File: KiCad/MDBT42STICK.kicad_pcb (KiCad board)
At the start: 2 copper layers, 78.4 x 40 mm, 22 parts, among them P1 CONN_01X04, P12 SERIALBUS, P2 USB_B, P3 CONN_01X07, P4 CONN_01X01, P5 CONN_01X03, SW1 RESET, U1 ADMP401Module, U2 MDBT42, U3 addressableLEDchip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

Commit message: 2nd version.
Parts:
- removed the C1 at (76.6, 78.7)
- removed C5: 0.1uF, Capacitors_SMD:C_0603
- removed P12: SERIALBUS, library:SolderWirePad_Circle_5xInline_0-8mmDrill
- removed the P2 at (116.2, 81.9)
- removed the P3 at (87.8, 89.9)
- removed P5: CONN_01X03, TO_SOT_Packages_THT:TO-43_3Pin
- removed SW1: RESET, Pin_Headers:Pin_Header_Straight_1x02
- removed U9: addressableLEDchip, library:addressableLEDchip3535
- added C1: 0.1uF, Capacitors_SMD:C_0603, F.Cu at (78.2, 79.3)
- added C1: 0.1, Capacitors_SMD:C_0603, F.Cu at (4.79, 74.9)
- added C2: 10, Capacitors_SMD:C_0603, F.Cu at (4.79, 88.5)
- added OSHW: 1.1, library:OSHW_LOGL_SYLK_5mm, F.Cu at (127.7, 82.5)
- added OSHW: 1.1, library:OSHW_LOGL_SYLK_5mm, F.Cu at (139.1, 82.7)
- added OSHW: 1.1, library:OSHW_LOGL_SYLK_5mm, F.Cu at (-6.41, 81.7)
- added P1: CONN_01X10, Connectors_Molex:Connector_Molex_PicoBlade_53047-1010, F.Cu at (-0.41, 75.7)
- added P2: CONN_01X08, library:SolderWirePad_Circle_8xInline_0-85mmDrill, F.Cu at (80.1, 87.6)
- added P2: CONN_01X05, Connectors_Molex:Connector_Molex_PicoBlade_53047-0510, F.Cu at (10.2, 89.9)
- added P3: OLED_0.96in_SPI, library:SolderWirePad_Circle_7xInline_0-85mmDrill, F.Cu at (61.0, 77.4)
- added P3: CONN_01X04, library:Grove_I2C_Horisontal_4pin_2mmpitch, F.Cu at (13.6, 81.7)
- added R1: 4.7k, Resistors_SMD:R_0603, F.Cu at (12.2, 72.9)
- added R2: 4.7k, Resistors_SMD:R_0603, F.Cu at (12.2, 75.1)
- added R3: 1.8k, Resistors_SMD:R_0603, F.Cu at (15.8, 72.9)
- added R4: 1.8k, Resistors_SMD:R_0603, F.Cu at (15.8, 75.1)
- added R5: 20k, Resistors_SMD:R_0603, F.Cu at (6.39, 90.7)
- added REF**: SolderWirePad_single_1-2mmDrill, Wire_Pads:SolderWirePad_single_1-2mmDrill, F.Cu at (26.1, 81.9)
- added U1: MTCH6102_SSOP28, Housings_SSOP:TSSOP-28_4.4x9.7mm_Pitch0.65mm, F.Cu at (6.59, 81.7)
- added U4: CP2102_Module, library:CP2102Module, F.Cu at (40.4, 82.2)
- C3, C4: footprint library:C_1206_HandSoldering_Small -> Capacitors_SMD:C_0603
- D1: footprint Diodes_SMD:MELF_Standard -> Diodes_SMD:TUMD2
- U5: value MPU-6500_Module -> GY-LSM6DS3Module; footprint library:MPU-6500_GY-6500 -> library:GY-LSM6DS3Module
- moved U6 68.9 mm to (36.6, 82.2), turned to 0 degrees
- moved U3 56.6 mm to (51.1, 71.2), turned to 0 degrees
- moved BT1 52.1 mm to (53.4, 85.1)
- moved C3 47.5 mm to (59.3, 79.9)
- moved U7 41.1 mm to (54.4, 81.7), turned to 90 degrees
- moved U1 25.4 mm to (73.7, 82.5), turned to 270 degrees
- moved C4 20.8 mm to (75.1, 79.3), turned to 0 degrees
- moved P1 10.4 mm to (71.2, 77.4)
- moved SP1 9.03 mm to (64.6, 83.2), turned to 90 degrees
- moved P4 7.73 mm to (59.1, 82.5)
- moved D1 6.02 mm to (58.8, 85.7)
- moved U5 4.79 mm to (61.0, 82.5), turned to 90 degrees
- moved U8 1.80 mm to (75.0, 83.1)
- moved U2 1.37 mm to (87.0, 81.2)
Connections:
- BT1 pad 2: GND -> Net-(BT1-Pad2)
- D1 pad 1: Net-(BT1-Pad1) -> Net-(D1-Pad1)
- D1 pad 2: Net-(D1-Pad2) -> Net-(BT1-Pad2)
- P4 pad 1: Net-(D1-Pad2) -> Net-(D1-Pad1)
- U2 pad 30: Net-(P12-Pad2) -> Net-(SW1-Pad2)
- U2 pad 35: Net-(SW1-Pad2) -> Net-(U2-Pad35)
- U5 pad 1: +3V3 -> Net-(BT1-Pad1)
- U5 pad 2: GND -> +3V3
- U5 pad 3: Net-(U2-Pad20) -> GND
- U5 pad 4: Net-(U2-Pad31) -> Net-(U2-Pad20)
- U5 pad 5: Net-(U5-Pad5) -> Net-(U2-Pad31)
- U5 pad 6: Net-(U5-Pad6) -> Net-(U2-Pad17)
- U5 pad 7: Net-(U5-Pad7) -> Net-(U2-Pad16)
- U6 pad 1: +5V -> Net-(U4-Pad3)
- U6 pad 4: GND -> Net-(BT1-Pad1)
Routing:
- net Net-(U2-Pad35): track 0.00 -> 49.9 mm, vias 0 -> 1
- net +3V3: track 113.0 -> 66.0 mm, vias 6 -> 1
- net Net-(P3-Pad3): track 29.0 -> 74.1 mm, vias 2 -> 4
- net Net-(C1-Pad1): track 0.00 -> 44.9 mm, vias 0 -> 2
- net Net-(SW1-Pad2): track 35.9 -> 0.00 mm, vias 4 -> 0
- net Net-(C1-Pad2): track 0.00 -> 34.6 mm
- net GND: track 174.0 -> 139.6 mm, vias 5 -> 10
- net Net-(BT1-Pad1): track 57.5 -> 25.6 mm, vias 1 -> 0
- net Net-(U2-Pad29): track 16.5 -> 46.3 mm
- net Net-(U4-Pad3): track 0.00 -> 28.9 mm
- net Net-(U2-Pad17): track 0.00 -> 27.8 mm, vias 0 -> 1
- net Net-(P3-Pad4): track 29.7 -> 57.0 mm, vias 2 -> 3
- net Net-(U2-Pad16): track 0.00 -> 26.7 mm, vias 0 -> 1
- net Net-(P2-Pad5): track 10.2 -> 33.3 mm, vias 2 -> 3
- net Net-(P2-Pad1): track 14.1 -> 35.5 mm, vias 1 -> 2
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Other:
- board size 78.4 x 40 mm -> 159 x 31 mm
- board text added: "00SCL 03SDA 06CS 08SA0"
- board text added: "01 03A1 04A2 05A3 07 09 10 11"
- board text added: "3V3 GND"
- board text added: "3V3 GND +5V ▲RX ▼TX DTR"
- board text added: "3V3 GND +5V ▼RX ▲TX DTR"
- board text added: "B+ B-"
- board text added: "CLK 3V3 DIO GND"
- board text added: "GND SIO 3.3 CLK"
- board text added: "MISO MOSI"
- board text added: "SCL MISO RST MOSI SCK"
- board text added: "SPI OLED Module"
- board text added: "ST-Link"
- board text added: "VIN 3V3 GND"
- board text added: "▼31A7"
- board text added: "▼Breadboard"
- board text added: "▼GYLOModule"
- board text added: "▼Speaker"
- board text removed: "GND 3V3 5NC RX TX"
- board text removed: "GND CLK 3.3 SIO"

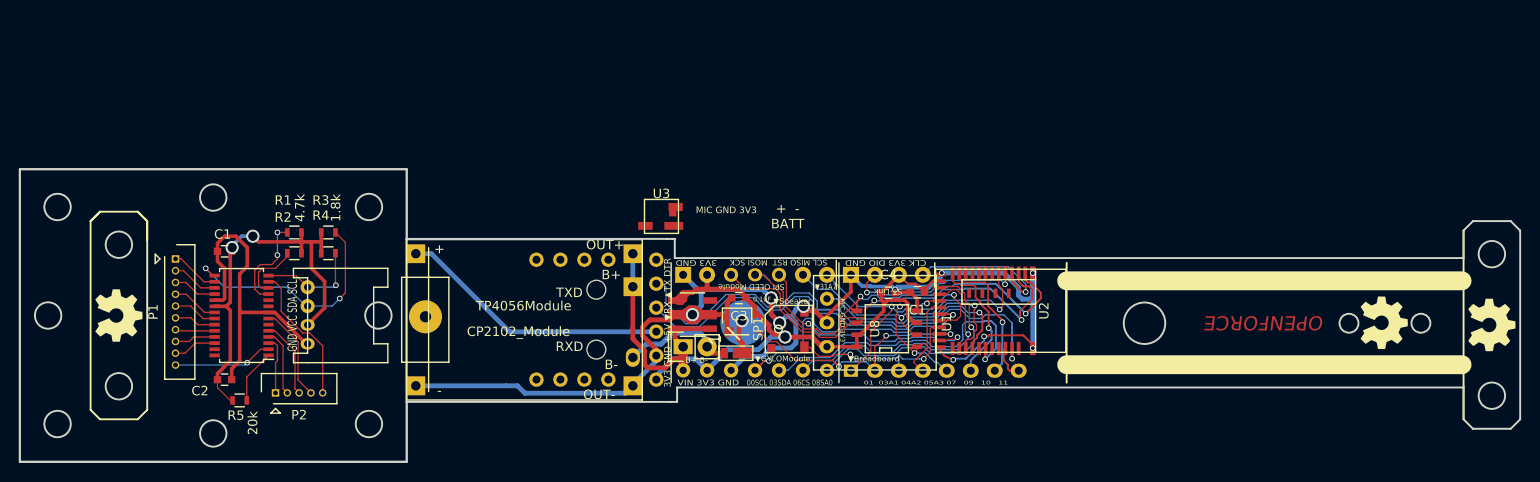
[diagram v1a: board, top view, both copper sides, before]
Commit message: 20180525 Version. Size Reduce.
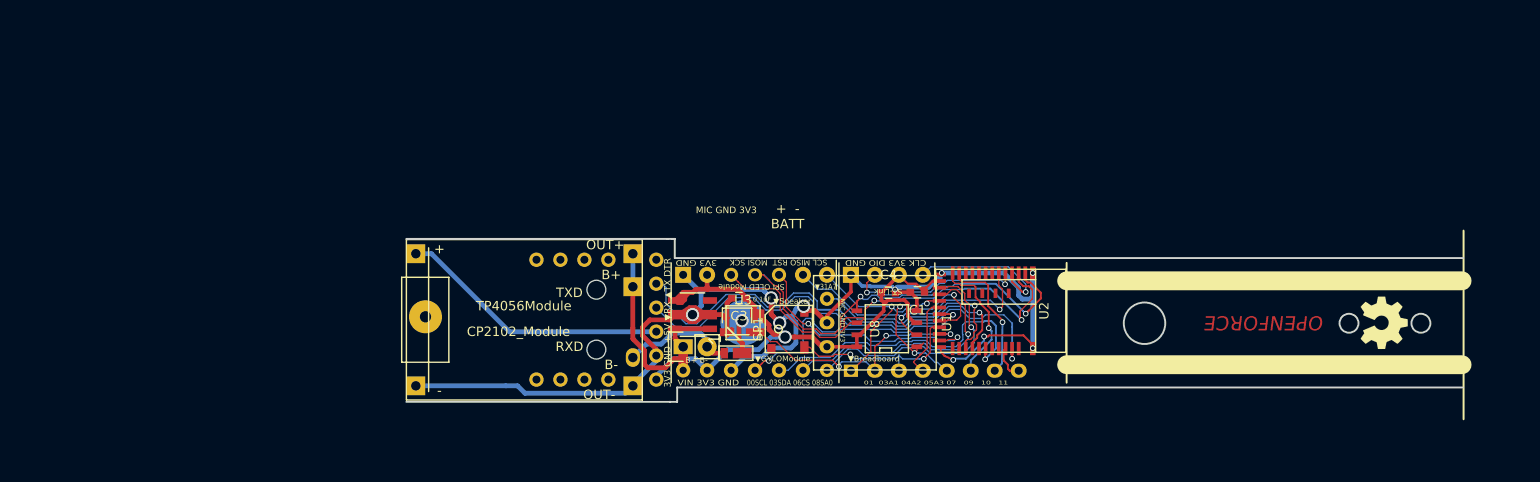
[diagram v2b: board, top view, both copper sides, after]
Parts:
- removed the C1 at (4.79, 74.9)
- removed C2: 10, Capacitors_SMD:C_0603
- removed the OSHW at (139.1, 82.7)
- removed the OSHW at (-6.41, 81.7)
- removed the P1 at (-0.41, 75.7)
- removed the P2 at (10.2, 89.9)
- removed the P3 at (13.6, 81.7)
- removed R1, R2: 4.7k, Resistors_SMD:R_0603
- removed R3, R4: 1.8k, Resistors_SMD:R_0603
- removed R5: 20k, Resistors_SMD:R_0603
- removed the U1 at (6.59, 81.7)
- moved U3 14.2 mm to (59.7, 82.5)
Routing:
- net Net-(C1-Pad1): track 44.9 -> 0.00 mm, vias 2 -> 0
- net Net-(C1-Pad2): track 34.6 -> 0.00 mm
- net Net-(P3-Pad3): track 74.1 -> 48.9 mm, vias 4 -> 2
- net Net-(P2-Pad5): track 33.3 -> 18.3 mm
- net Net-(P3-Pad4): track 57.0 -> 45.8 mm, vias 3 -> 2
- net Net-(P1-Pad10): track 10.5 -> 0.00 mm, vias 1 -> 0
- net Net-(R1-Pad2): track 10.5 -> 0.00 mm, vias 2 -> 0
- net Net-(P2-Pad4): track 19.0 -> 8.83 mm
- net Net-(P2-Pad3): track 28.7 -> 20.4 mm
- net Net-(P2-Pad2): track 34.6 -> 27.5 mm
- net Net-(R2-Pad2): track 6.82 -> 0.00 mm
- net Net-(R5-Pad2): track 6.43 -> 0.00 mm
- net Net-(P2-Pad1): track 35.5 -> 29.4 mm
- net Net-(P1-Pad1): track 5.15 -> 0.00 mm
- net Net-(P1-Pad4): track 20.6 -> 15.7 mm
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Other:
- board size 159 x 31 mm -> 112 x 17.3 mm

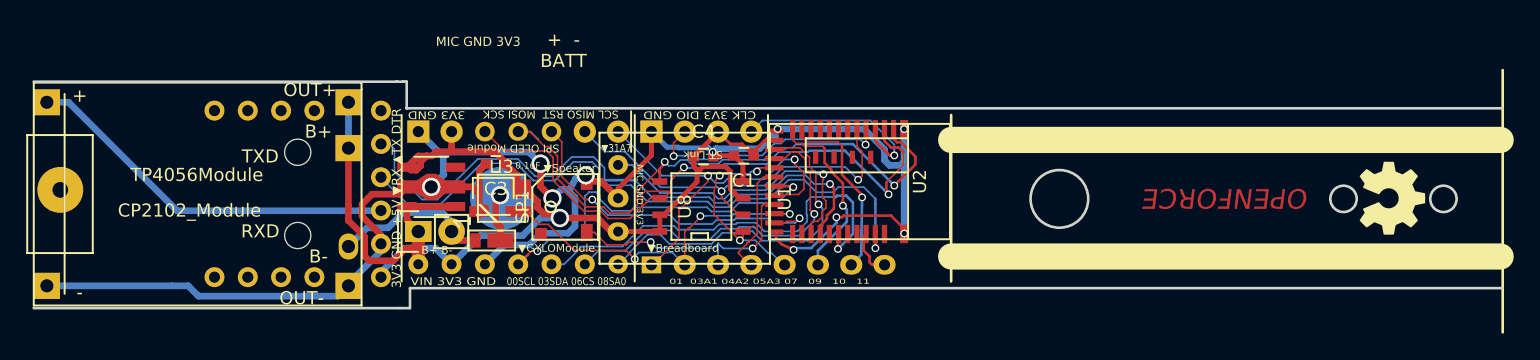
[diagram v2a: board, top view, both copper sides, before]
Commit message: 20180727 Version. Documents add and modify full color LED.
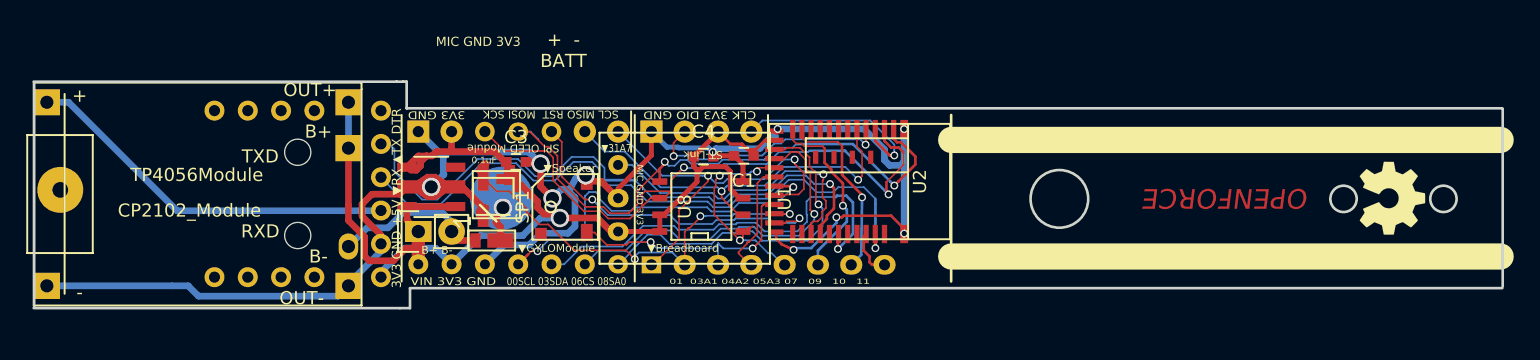
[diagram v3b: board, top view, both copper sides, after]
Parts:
- moved C3 1.54 mm to (60.8, 79.7), turned to 0 degrees
- moved U3 0.48 mm to (59.3, 82.2), turned to 270 degrees
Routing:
- net Net-(P2-Pad2): track 27.5 -> 32.3 mm
- net GND: track 139.6 -> 138.2 mm
- net Net-(D1-Pad1): track 4.06 -> 3.14 mm
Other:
- outline, holes or cut-outs redrawn
- board text added: "AONODON20180727"
